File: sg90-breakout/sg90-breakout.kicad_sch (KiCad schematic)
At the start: 3 parts, among them J1 Conn_01x03, J2 Conn_01x05_MountingPin, M1 Motor_DC

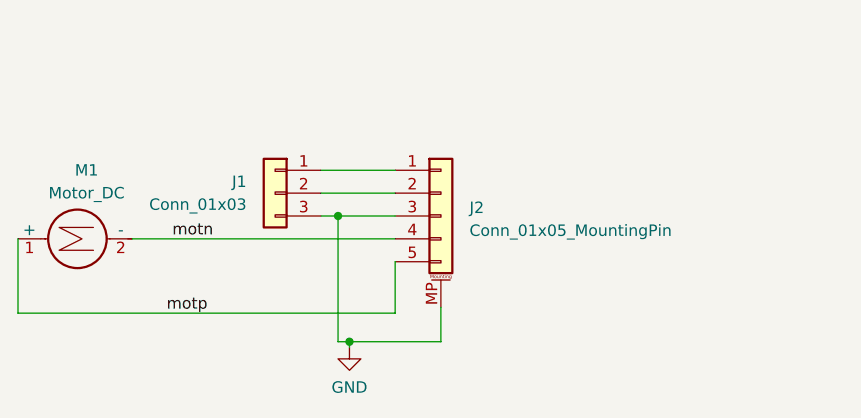
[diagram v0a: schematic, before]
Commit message: vertical and horizontal connector footprints
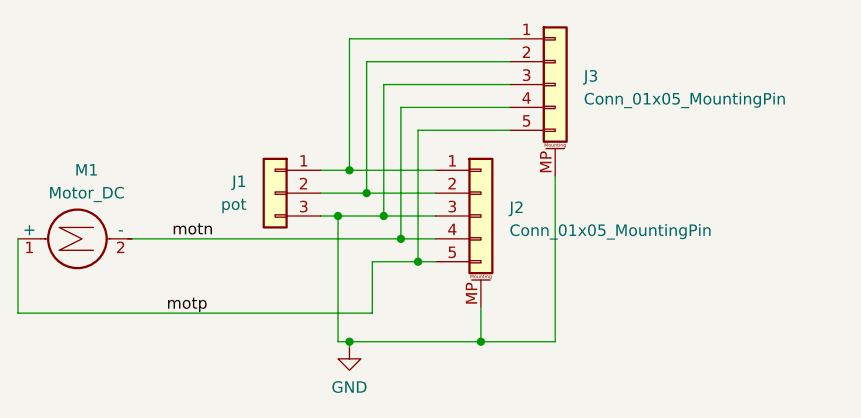
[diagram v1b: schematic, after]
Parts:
- added J3: Conn_01x05_MountingPin, Connector_JST:JST_SH_SM05B-SRSS-TB_1x05-1MP_P1.00mm_Horizontal, symbol Connector_Generic_MountingPin:Conn_01x05_MountingPin
- J1: value Conn_01x03 -> pot
- J2: footprint Connector_JST:JST_SH_SM05B-SRSS-TB_1x05-1MP_P1.00mm_Horizontal -> Connector_JST:JST_SH_BM05B-SRSS-TB_1x05-1MP_P1.00mm_Vertical
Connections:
- net GND: now also J3.3 (Pin_3), J3.MP (MountPin)
- net motn: now also J3.4 (Pin_4)
- net motp: now also J3.5 (Pin_5)
- net at J1.1 (Pin_1), J2.1 (Pin_1): now also J3.1 (Pin_1)
- net at J1.2 (Pin_2), J2.2 (Pin_2): now also J3.2 (Pin_2)
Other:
- moved on the sheet: J2
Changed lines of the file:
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@@
 (kicad_sch (version 20230121) (generator eeschema)
   (paper "USLetter")
+  (junction (at 157.48 101.6) (diameter 0) (color 0 0 0 0)
+  )
   (junction (at 151.765 113.03) (diameter 0) (color 0 0 0 0)
   )
+  (junction (at 155.575 99.06) (diameter 0) (color 0 0 0 0)
+  )
+  (junction (at 153.67 96.52) (diameter 0) (color 0 0 0 0)
+  )
+  (junction (at 166.37 113.03) (diameter 0) (color 0 0 0 0)
+  )
   (junction (at 150.495 99.06) (diameter 0) (color 0 0 0 0)
   )
+  (junction (at 151.765 93.98) (diameter 0) (color 0 0 0 0)
+  )
+  (junction (at 159.385 104.14) (diameter 0) (color 0 0 0 0)
+  )
+  (wire (pts (xy 153.67 81.915) (xy 153.67 96.52))
+    (stroke (width 0) (type default))
+  )
+  (wire (pts (xy 148.59 93.98) (xy 151.765 93.98))
+    (stroke (width 0) (type default))
+  )
   (wire (pts (xy 150.495 99.06) (xy 150.495 113.03))
     (stroke (width 0) (type default))
   )
+  (wire (pts (xy 169.545 89.535) (xy 159.385 89.535))
+    (stroke (width 0) (type default))
+  )
   (wire (pts (xy 150.495 113.03) (xy 151.765 113.03))
     (stroke (width 0) (type default))
   )
-  (wire (pts (xy 148.59 96.52) (xy 156.845 96.52))
-    (stroke (width 0) (type default))
-  )
-  (wire (pts (xy 151.765 113.03) (xy 161.925 113.03))
-    (stroke (width 0) (type default))
-  )
-  (wire (pts (xy 161.925 113.03) (xy 161.925 109.22))
+  (wire (pts (xy 155.575 99.06) (xy 161.29 99.06))
+    (stroke (width 0) (type default))
+  )
+  (wire (pts (xy 169.545 86.995) (xy 157.48 86.995))
+    (stroke (width 0) (type default))
+  )
+  (wire (pts (xy 153.67 96.52) (xy 161.29 96.52))
+    (stroke (width 0) (type default))
+  )
+  (wire (pts (xy 174.625 94.615) (xy 174.625 113.03))
+    (stroke (width 0) (type default))
+  )
+  (wire (pts (xy 151.765 113.03) (xy 166.37 113.03))
+    (stroke (width 0) (type default))
+  )
+  (wire (pts (xy 169.545 79.375) (xy 151.765 79.375))
+    (stroke (width 0) (type default))
+  )
+  (wire (pts (xy 151.765 93.98) (xy 161.29 93.98))
+    (stroke (width 0) (type default))
+  )
+  (wire (pts (xy 159.385 104.14) (xy 154.305 104.14))
+    (stroke (width 0) (type default))
+  )
+  (wire (pts (xy 166.37 113.03) (xy 166.37 109.22))
     (stroke (width 0) (type default))
   )
@@
     (stroke (width 0) (type default))
   )
+  (wire (pts (xy 157.48 86.995) (xy 157.48 101.6))
+    (stroke (width 0) (type default))
+  )
+  (wire (pts (xy 166.37 113.03) (xy 174.625 113.03))
+    (stroke (width 0) (type default))
+  )
+  (wire (pts (xy 155.575 84.455) (xy 155.575 99.06))
+    (stroke (width 0) (type default))
+  )
   (wire (pts (xy 114.935 109.855) (xy 114.935 101.6))
     (stroke (width 0) (type default))
   )
-  (wire (pts (xy 150.495 99.06) (xy 156.845 99.06))
-    (stroke (width 0) (type default))
-  )
-  (wire (pts (xy 127.635 101.6) (xy 156.845 101.6))
-    (stroke (width 0) (type default))
-  )
-  (wire (pts (xy 114.935 109.855) (xy 156.845 109.855))
-    (stroke (width 0) (type default))
-  )
-  (wire (pts (xy 156.845 104.14) (xy 156.845 109.855))
+  (wire (pts (xy 150.495 99.06) (xy 155.575 99.06))
+    (stroke (width 0) (type default))
+  )
+  (wire (pts (xy 159.385 104.14) (xy 161.29 104.14))
+    (stroke (width 0) (type default))
+  )
+  (wire (pts (xy 127.635 101.6) (xy 157.48 101.6))
+    (stroke (width 0) (type default))
+  )
+  (wire (pts (xy 148.59 96.52) (xy 153.67 96.52))
+    (stroke (width 0) (type default))
+  )
+  (wire (pts (xy 159.385 89.535) (xy 159.385 104.14))
+    (stroke (width 0) (type default))
+  )
+  (wire (pts (xy 169.545 84.455) (xy 155.575 84.455))
+    (stroke (width 0) (type default))
+  )
+  (wire (pts (xy 169.545 81.915) (xy 153.67 81.915))
+    (stroke (width 0) (type default))
+  )
+  (wire (pts (xy 114.935 109.855) (xy 154.305 109.855))
+    (stroke (width 0) (type default))
+  )
+  (wire (pts (xy 154.305 104.14) (xy 154.305 109.855))
     (stroke (width 0) (type default))
   )
@@
     (stroke (width 0) (type default))
   )
-  (wire (pts (xy 148.59 93.98) (xy 156.845 93.98))
+  (wire (pts (xy 151.765 79.375) (xy 151.765 93.98))
+    (stroke (width 0) (type default))
+  )
+  (wire (pts (xy 157.48 101.6) (xy 161.29 101.6))
     (stroke (width 0) (type default))
   )
@@
     (effects (font (size 1.27 1.27)) (justify left bottom))
   )
-  (symbol (lib_id "Connector_Generic_MountingPin:Conn_01x05_MountingPin") (at 161.925 99.06 0) (unit 1)
-    (in_bom yes) (on_board yes) (dnp no) (fields_autoplaced)
-    (property "Reference" "J2" (at 165.1 98.1456 0)
-      (effects (font (size 1.27 1.27)) (justify left))
-    )
-    (property "Value" "Conn_01x05_MountingPin" (at 165.1 100.6856 0)
-      (effects (font (size 1.27 1.27)) (justify left))
-    )
-    (property "Footprint" "Connector_JST:JST_SH_SM05B-SRSS-TB_1x05-1MP_P1.00mm_Horizontal" (at 161.925 99.06 0)
-      (effects (font (size 1.27 1.27)) hide)
-    )
-    (property "Datasheet" "~" (at 161.925 99.06 0)
+  (symbol (lib_id "Connector_Generic_MountingPin:Conn_01x05_MountingPin") (at 166.37 99.06 0) (unit 1)
+    (in_bom yes) (on_board yes) (dnp no) (fields_autoplaced)
+    (property "Reference" "J2" (at 169.545 98.1456 0)
+      (effects (font (size 1.27 1.27)) (justify left))
+    )
+    (property "Value" "Conn_01x05_MountingPin" (at 169.545 100.6856 0)
+      (effects (font (size 1.27 1.27)) (justify left))
+    )
+    (property "Footprint" "Connector_JST:JST_SH_BM05B-SRSS-TB_1x05-1MP_P1.00mm_Vertical" (at 166.37 99.06 0)
+      (effects (font (size 1.27 1.27)) hide)
+    )
+    (property "Datasheet" "~" (at 166.37 99.06 0)
       (effects (font (size 1.27 1.27)) hide)
     )
@@
       (effects (font (size 1.27 1.27)) (justify left))
     )
-    (property "Value" "Conn_01x03" (at 140.335 97.79 0)
+    (property "Value" "pot" (at 140.335 97.79 0)
       (effects (font (size 1.27 1.27)) (justify left))
     )
@@
         )
       )
+    )
+  )
+  (symbol (lib_id "Connector_Generic_MountingPin:Conn_01x05_MountingPin") (at 174.625 84.455 0) (unit 1)
+    (in_bom yes) (on_board yes) (dnp no) (fields_autoplaced)
+    (property "Reference" "J3" (at 177.8 83.5406 0)
+      (effects (font (size 1.27 1.27)) (justify left))
+    )
+    (property "Value" "Conn_01x05_MountingPin" (at 177.8 86.0806 0)
+      (effects (font (size 1.27 1.27)) (justify left))
+    )
+    (property "Footprint" "Connector_JST:JST_SH_SM05B-SRSS-TB_1x05-1MP_P1.00mm_Horizontal" (at 174.625 84.455 0)
+      (effects (font (size 1.27 1.27)) hide)
+    )
+    (property "Datasheet" "~" (at 174.625 84.455 0)
+      (effects (font (size 1.27 1.27)) hide)
+    )
+    (pin "5")
+    (pin "3")
+    (pin "2")
+    (pin "1")
+    (pin "MP")
+    (pin "4")
+    (instances
+      (project "sg90-breakout"
+        (path "/e251905f-09d3-4b82-b4ef-bdd184ccc61f"
+          (reference "J3") (unit 1)
+        )
+      )

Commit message: Renumber pins to match rotations
Viewed from top:
* counter-clockwise is increasing pulse-width for normal servo
* positive P-N to motor gives CCW output rotation
* CCW rotation moves pot wiper towards "top" of pot
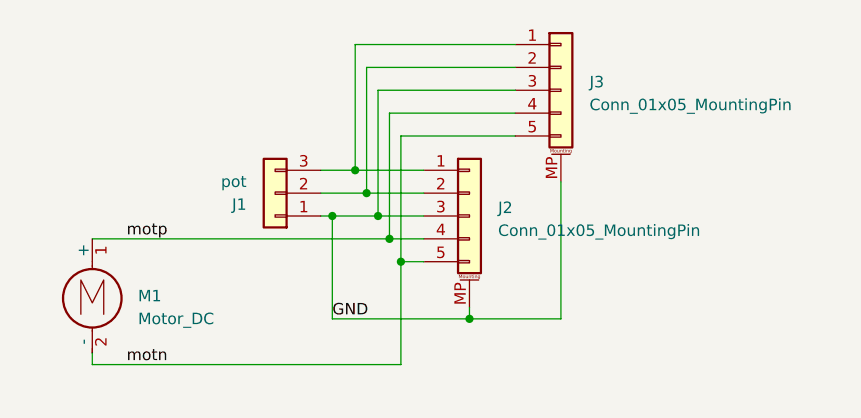
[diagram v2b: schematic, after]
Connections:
- net GND: now also J1.1 (Pin_1); no longer J1.3 (Pin_3)
- net motn: now also J2.5 (Pin_5), J3.5 (Pin_5); no longer J2.4 (Pin_4), J3.4 (Pin_4)
- net motp: now also J2.4 (Pin_4), J3.4 (Pin_4); no longer J2.5 (Pin_5), J3.5 (Pin_5)
- net at J2.1 (Pin_1), J3.1 (Pin_1): now also J1.3 (Pin_3); no longer J1.1 (Pin_1)
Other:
- moved on the sheet: J1, J2, J3, M1
